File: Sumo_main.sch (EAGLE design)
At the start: 25 parts, among them U1 ATMEGA8U2AU, X1 MINI-USB-SCHIELD-32005-201, X2 ESC1, X3 ESC2, X4 IR Sensor 1, X5 IR Sensor 2, X6 IR Sensor 3, Y1 4MHz

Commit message: Added RS-485
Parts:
- removed X3: ESC2, con-amp-micromatch:MICROMATCH-4
- added C5: 10uF, SparkFun-Capacitors:CAP0603-CAP
- added IC1: MAX3469ESA, maxim:MAX3469ESA
- added R8: 22R, resistor:R-EU_R0603
- X2: value ESC1 -> RS485
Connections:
- new net DE: IC1.DE, IC1.RE/, U1.PD4
- new net N$11: IC1.B, R8.2, X2-4.S
- new net N$12: IC1.A, R8.1, X2-3.S
- new net N$15: C5.1, X2-2.S
- new net RX: IC1.RO, U1.PD2(RX)
- new net TX: IC1.DI, U1.PD3(TX)
- new net V01: U1.PD0, X4-1.S
- new net V02: U1.PD1, X5-1.S
- new net V03: U1.PD5, X6-1.S
- net GND: now also IC1.GND, X2-1.S, X4-2.S, X5-2.S, X6-2.S
- net VCC: now also C5.2, IC1.VCC, X4-3.S, X5-3.S, X6-3.S
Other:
- moved on the sheet: C1, D1, D2, D3, F1, R1, R2, R4, R5, R7, X1G$1, X1S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

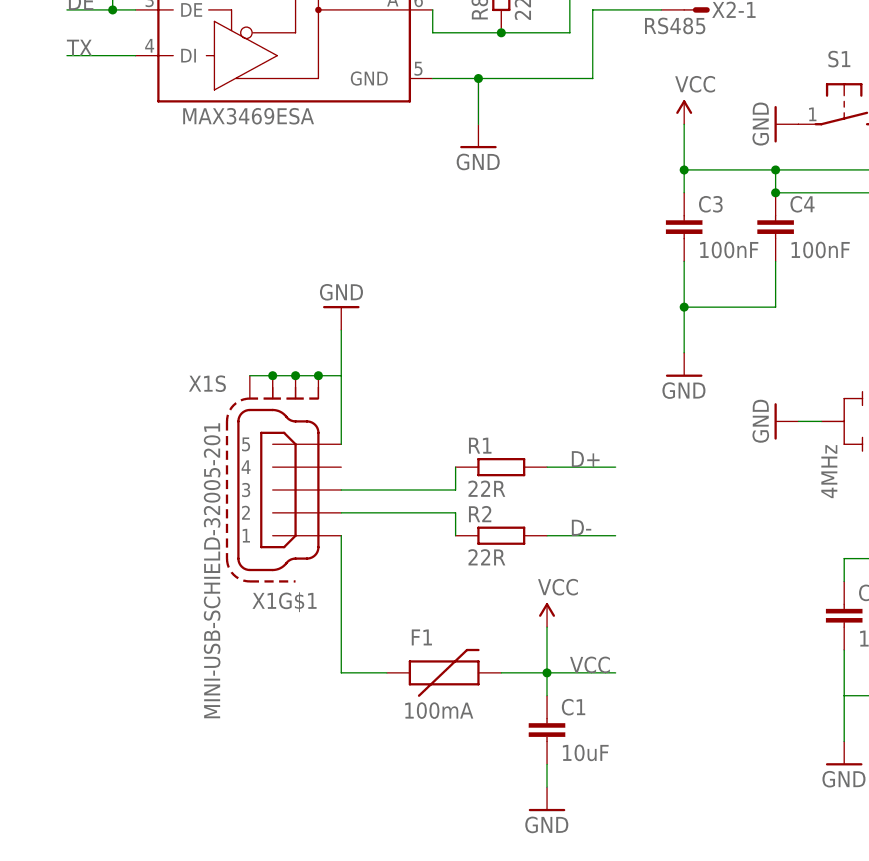
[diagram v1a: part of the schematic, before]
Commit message: Added Non-USB voltage supply.
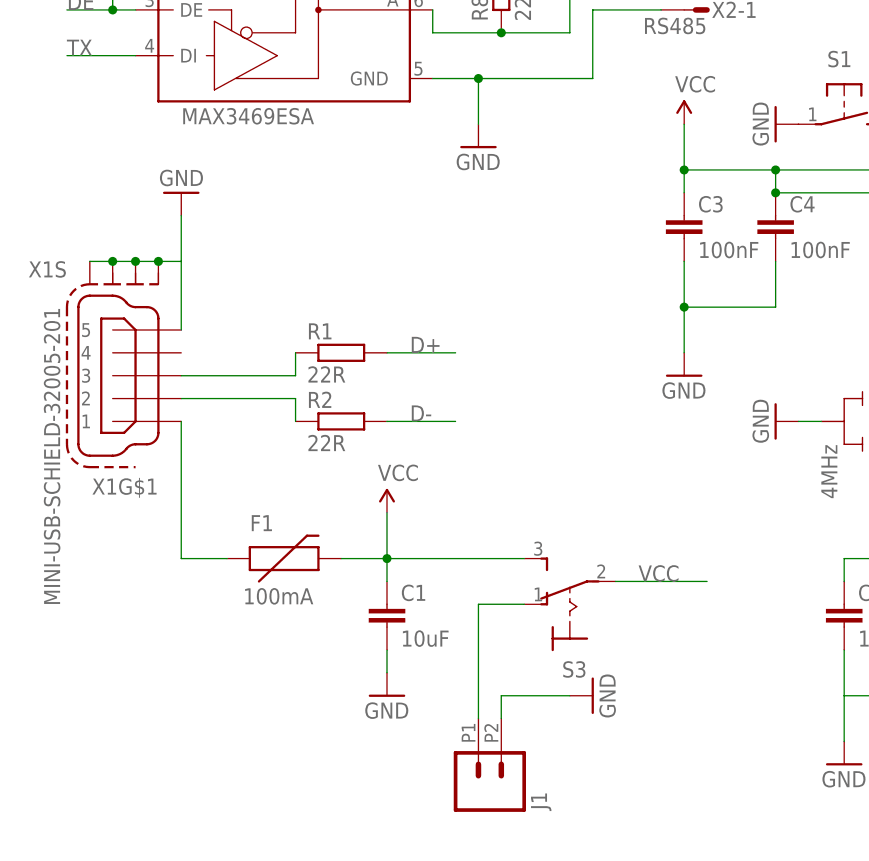
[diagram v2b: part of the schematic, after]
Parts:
- added J1: (no value), SparkFun-Connectors:M022.54MM_SCREWTERM
- added S3: (no value), switch:M9040P
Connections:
- new net N$14: J1.1, S3.O
- net GND: now also J1.2
- net VCC: now also S3.P, S3.S
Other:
- moved on the sheet: C1, F1, R1, R2, X1G$1, X1S
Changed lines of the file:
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@@
 <?xml version="1.0" encoding="utf-8"?>
 <!DOCTYPE eagle SYSTEM "eagle.dtd">
-<eagle version="7.1.0">
+<eagle version="6.5.0">
 <drawing>
 <settings>
@@
 <part name="C5" library="SparkFun-Capacitors" deviceset="CAP" device="0603-CAP" value="10uF"/>
 <part name="SUPPLY6" library="SparkFun-Aesthetics" deviceset="VCC" device=""/>
+<part name="J1" library="SparkFun-Connectors" deviceset="M02" device="2.54MM_SCREWTERM"/>
+<part name="GND10" library="SparkFun-Aesthetics" deviceset="GND" device=""/>
+<part name="S3" library="switch" deviceset="M9040P" device=""/>
 </parts>
 <sheets>
@@
 <instances>
 <instance part="U1" gate="G$1" x="73.66" y="58.42"/>
-<instance part="F1" gate="G$1" x="-5.08" y="25.4"/>
-<instance part="R1" gate="G$1" x="2.54" y="48.26"/>
-<instance part="R2" gate="G$1" x="2.54" y="40.64"/>
-<instance part="C1" gate="G$1" x="7.62" y="17.78"/>
+<instance part="F1" gate="G$1" x="-22.86" y="38.1"/>
+<instance part="R1" gate="G$1" x="-15.24" y="60.96"/>
+<instance part="R2" gate="G$1" x="-15.24" y="53.34"/>
+<instance part="C1" gate="G$1" x="-10.16" y="30.48"/>
 <instance part="C2" gate="G$1" x="40.64" y="30.48"/>
 <instance part="C3" gate="G$1" x="22.86" y="73.66"/>
 <instance part="C4" gate="G$1" x="33.02" y="73.66"/>
-<instance part="SUPPLY1" gate="G$1" x="7.62" y="30.48"/>
-<instance part="GND1" gate="1" x="7.62" y="10.16"/>
+<instance part="SUPPLY1" gate="G$1" x="-10.16" y="43.18"/>
+<instance part="GND1" gate="1" x="-10.16" y="22.86"/>
 <instance part="GND2" gate="1" x="40.64" y="15.24"/>
 <instance part="GND3" gate="1" x="33.02" y="53.34" rot="R270"/>
-<instance part="GND4" gate="1" x="-15.24" y="66.04" rot="R180"/>
-<instance part="X1" gate="G$1" x="-20.32" y="45.72" rot="R180"/>
-<instance part="X1" gate="S" x="-20.32" y="55.88" rot="R180"/>
+<instance part="GND4" gate="1" x="-33.02" y="78.74" rot="R180"/>
+<instance part="X1" gate="G$1" x="-38.1" y="58.42" rot="R180"/>
+<instance part="X1" gate="S" x="-38.1" y="68.58" rot="R180"/>
 <instance part="Y1" gate="G$1" x="45.72" y="53.34" rot="R270"/>
 <instance part="SUPPLY2" gate="G$1" x="22.86" y="86.36"/>
@@
 <instance part="C5" gate="G$1" x="20.32" y="114.3" rot="R90"/>
 <instance part="SUPPLY6" gate="G$1" x="25.4" y="114.3" rot="R270"/>
+<instance part="J1" gate="G$1" x="0" y="12.7" rot="MR90"/>
+<instance part="GND10" gate="1" x="12.7" y="22.86" rot="R90"/>
+<instance part="S3" gate="1" x="10.16" y="33.02" rot="R90"/>
 </instances>
 <busses>
@@
 <segment>
 <pinref part="R1" gate="G$1" pin="1"/>
-<wire x1="-2.54" y1="45.72" x2="-2.54" y2="48.26" width="0.1524" layer="91"/>
+<wire x1="-20.32" y1="58.42" x2="-20.32" y2="60.96" width="0.1524" layer="91"/>
 <pinref part="X1" gate="G$1" pin="3"/>
-<wire x1="-15.24" y1="45.72" x2="-2.54" y2="45.72" width="0.1524" layer="91"/>
+<wire x1="-33.02" y1="58.42" x2="-20.32" y2="58.42" width="0.1524" layer="91"/>
 </segment>
 </net>
@@
 <segment>
 <pinref part="R2" gate="G$1" pin="1"/>
-<wire x1="-15.24" y1="43.18" x2="-2.54" y2="43.18" width="0.1524" layer="91"/>
-<wire x1="-2.54" y1="43.18" x2="-2.54" y2="40.64" width="0.1524" layer="91"/>
+<wire x1="-33.02" y1="55.88" x2="-20.32" y2="55.88" width="0.1524" layer="91"/>
+<wire x1="-20.32" y1="55.88" x2="-20.32" y2="53.34" width="0.1524" layer="91"/>
 <pinref part="X1" gate="G$1" pin="2"/>
 </segment>
@@
 <segment>
 <pinref part="R1" gate="G$1" pin="2"/>
-<wire x1="7.62" y1="48.26" x2="15.24" y2="48.26" width="0.1524" layer="91"/>
-<label x="10.16" y="48.26" size="1.778" layer="95"/>
+<wire x1="-10.16" y1="60.96" x2="-2.54" y2="60.96" width="0.1524" layer="91"/>
+<label x="-7.62" y="60.96" size="1.778" layer="95"/>
 </segment>
 <segment>
@@
 <segment>
 <pinref part="R2" gate="G$1" pin="2"/>
-<wire x1="7.62" y1="40.64" x2="15.24" y2="40.64" width="0.1524" layer="91"/>
-<label x="10.16" y="40.64" size="1.778" layer="95"/>
+<wire x1="-10.16" y1="53.34" x2="-2.54" y2="53.34" width="0.1524" layer="91"/>
+<label x="-7.62" y="53.34" size="1.778" layer="95"/>
 </segment>
 <segment>
@@
 <net name="N$3" class="0">
 <segment>
-<wire x1="-15.24" y1="40.64" x2="-15.24" y2="25.4" width="0.1524" layer="91"/>
+<wire x1="-33.02" y1="53.34" x2="-33.02" y2="38.1" width="0.1524" layer="91"/>
 <pinref part="F1" gate="G$1" pin="1"/>
-<wire x1="-15.24" y1="25.4" x2="-10.16" y2="25.4" width="0.1524" layer="91"/>
+<wire x1="-33.02" y1="38.1" x2="-27.94" y2="38.1" width="0.1524" layer="91"/>
 <pinref part="X1" gate="G$1" pin="1"/>
 </segment>
@@
 <pinref part="F1" gate="G$1" pin="2"/>
 <pinref part="SUPPLY1" gate="G$1" pin="VCC"/>
-<wire x1="2.54" y1="25.4" x2="7.62" y2="25.4" width="0.1524" layer="91"/>
-<wire x1="7.62" y1="25.4" x2="7.62" y2="30.48" width="0.1524" layer="91"/>
+<wire x1="-15.24" y1="38.1" x2="-10.16" y2="38.1" width="0.1524" layer="91"/>
+<wire x1="-10.16" y1="38.1" x2="-10.16" y2="43.18" width="0.1524" layer="91"/>
 <pinref part="C1" gate="G$1" pin="1"/>
-<wire x1="7.62" y1="22.86" x2="7.62" y2="25.4" width="0.1524" layer="91"/>
-<wire x1="7.62" y1="25.4" x2="15.24" y2="25.4" width="0.1524" layer="91"/>
-<label x="10.16" y="25.4" size="1.778" layer="95"/>
-<junction x="7.62" y="25.4"/>
+<wire x1="-10.16" y1="35.56" x2="-10.16" y2="38.1" width="0.1524" layer="91"/>
+<junction x="-10.16" y="38.1"/>
+<pinref part="S3" gate="1" pin="S"/>
+<wire x1="-10.16" y1="38.1" x2="5.08" y2="38.1" width="0.1524" layer="91"/>
 </segment>
 <segment>
@@
 <junction x="25.4" y="114.3"/>
 </segment>
+<segment>
+<pinref part="S3" gate="1" pin="P"/>
+<wire x1="15.24" y1="35.56" x2="25.4" y2="35.56" width="0.1524" layer="91"/>
+<label x="17.78" y="35.56" size="1.778" layer="95"/>
+</segment>
 </net>
 <net name="GND" class="0">
@@
 <pinref part="C1" gate="G$1" pin="2"/>
 <pinref part="GND1" gate="1" pin="GND"/>
-<wire x1="7.62" y1="15.24" x2="7.62" y2="12.7" width="0.1524" layer="91"/>
+<wire x1="-10.16" y1="27.94" x2="-10.16" y2="25.4" width="0.1524" layer="91"/>
 </segment>
 <segment>
 <pinref part="X1" gate="G$1" pin="5"/>
-<wire x1="-15.24" y1="50.8" x2="-15.24" y2="58.42" width="0.1524" layer="91"/>
+<wire x1="-33.02" y1="63.5" x2="-33.02" y2="71.12" width="0.1524" layer="91"/>
 <pinref part="X1" gate="S" pin="S1"/>
-<wire x1="-15.24" y1="58.42" x2="-17.78" y2="58.42" width="0.1524" layer="91"/>
+<wire x1="-33.02" y1="71.12" x2="-35.56" y2="71.12" width="0.1524" layer="91"/>
 <pinref part="X1" gate="S" pin="S2"/>
 <pinref part="X1" gate="S" pin="S3"/>
 <pinref part="X1" gate="S" pin="S4"/>
-<wire x1="-25.4" y1="58.42" x2="-22.86" y2="58.42" width="0.1524" layer="91"/>
-<wire x1="-22.86" y1="58.42" x2="-20.32" y2="58.42" width="0.1524" layer="91"/>
-<wire x1="-20.32" y1="58.42" x2="-17.78" y2="58.42" width="0.1524" layer="91"/>
-<wire x1="-15.24" y1="58.42" x2="-15.24" y2="63.5" width="0.1524" layer="91"/>
-<junction x="-22.86" y="58.42"/>
-<junction x="-20.32" y="58.42"/>
-<junction x="-17.78" y="58.42"/>
+<wire x1="-43.18" y1="71.12" x2="-40.64" y2="71.12" width="0.1524" layer="91"/>
+<wire x1="-40.64" y1="71.12" x2="-38.1" y2="71.12" width="0.1524" layer="91"/>
+<wire x1="-38.1" y1="71.12" x2="-35.56" y2="71.12" width="0.1524" layer="91"/>
+<wire x1="-33.02" y1="71.12" x2="-33.02" y2="76.2" width="0.1524" layer="91"/>
+<junction x="-40.64" y="71.12"/>
+<junction x="-38.1" y="71.12"/>
+<junction x="-35.56" y="71.12"/>
 <pinref part="GND4" gate="1" pin="GND"/>
 </segment>
@@
 <wire x1="12.7" y1="99.06" x2="12.7" y2="91.44" width="0.1524" layer="91"/>
 </segment>
+<segment>
+<pinref part="J1" gate="G$1" pin="2"/>
+<pinref part="GND10" gate="1" pin="GND"/>
+<wire x1="2.54" y1="20.32" x2="2.54" y2="22.86" width="0.1524" layer="91"/>
+<wire x1="2.54" y1="22.86" x2="10.16" y2="22.86" width="0.1524" layer="91"/>
+</segment>
 </net>
 <net name="N$5" class="0">
@@
 </segment>
 </net>
+<net name="N$14" class="0">
+<segment>
+<pinref part="J1" gate="G$1" pin="1"/>
+<wire x1="0" y1="20.32" x2="0" y2="33.02" width="0.1524" layer="91"/>
+<pinref part="S3" gate="1" pin="O"/>
+<wire x1="0" y1="33.02" x2="5.08" y2="33.02" width="0.1524" layer="91"/>
+</segment>
+</net>

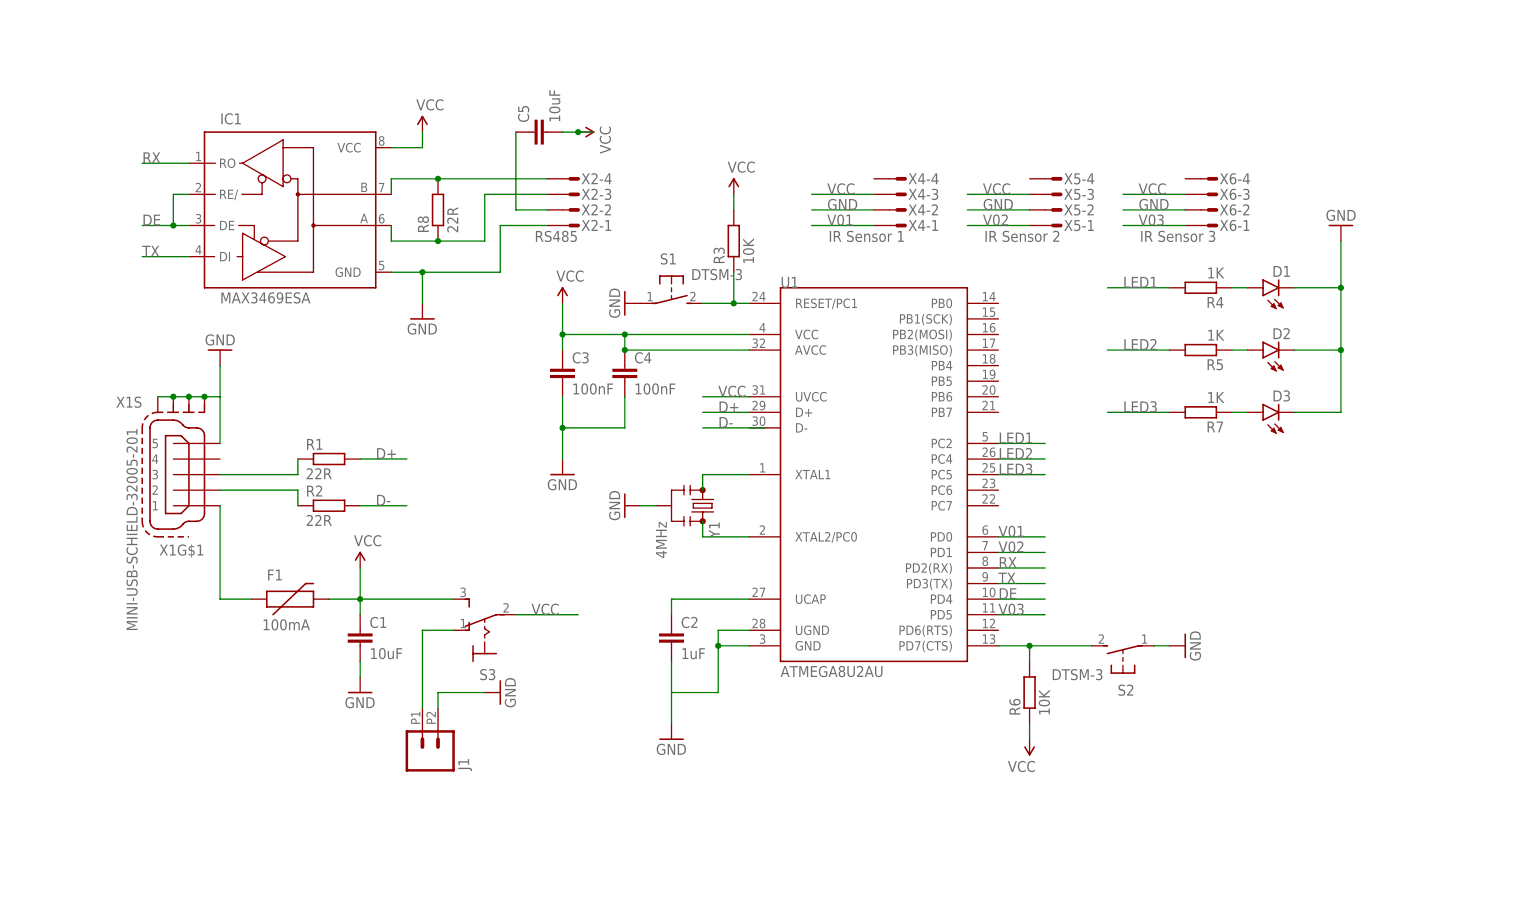
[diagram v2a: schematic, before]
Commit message: Changed RS485 module, added start module and power voltage regulator.
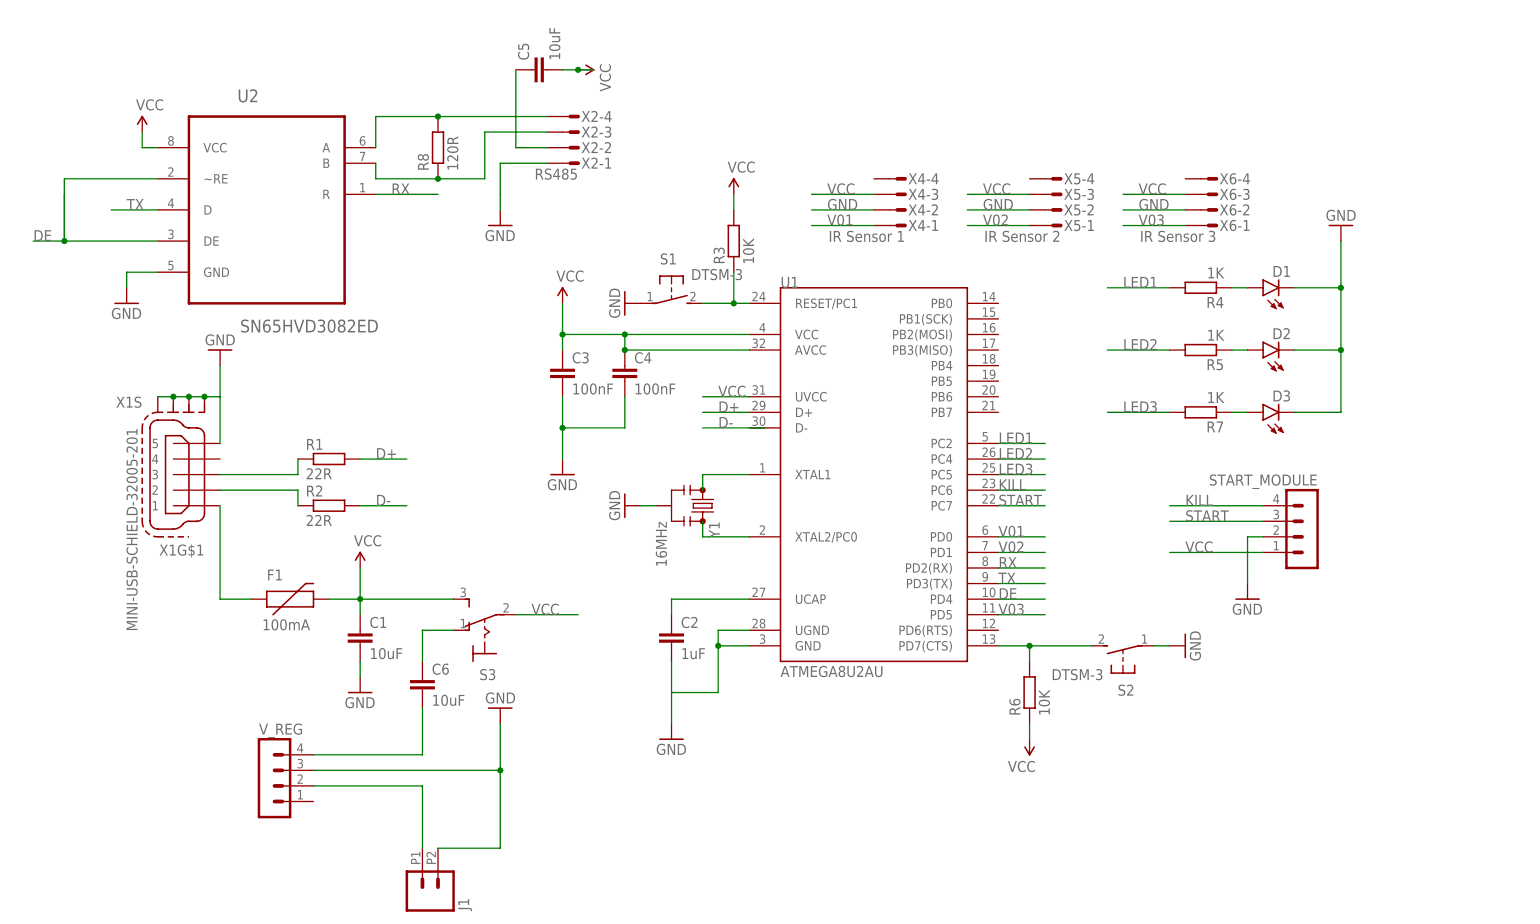
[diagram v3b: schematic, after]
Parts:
- removed IC1: MAX3469ESA, maxim:MAX3469ESA
- added C6: 10uF, SparkFun-Capacitors:CAP0603-CAP
- added START_MODULE, V_REG: (no value), con-lstb:MA04-1
- added U2: SN65HVD3082ED, SN65HVD3082ED:SN65HVD3082ED
- R8: value 22R -> 120R
- Y1: value 4MHz -> 16MHz
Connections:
- new net KILL: START_MODULE.4, U1.PC6
- new net N$21: C6.2, V_REG.4
- new net N$23: J1.1, V_REG.2
- new net START: START_MODULE.3, U1.PC7
- net DE: now also U2.DE, U2.~RE; no longer IC1.DE, IC1.RE/
- net GND: now also START_MODULE.2, U2.GND, V_REG.3; no longer IC1.GND
- net N$11: no longer IC1.B
- net N$12: no longer IC1.A
- net N$14: now also C6.1; no longer J1.1
- net RX: now also U2.R; no longer IC1.RO
- net TX: now also U2.D; no longer IC1.DI
- net VCC: now also START_MODULE.1, U2.VCC; no longer IC1.VCC
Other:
- moved on the sheet: C5, J1, R8, X2-1, X2-2, X2-3, X2-4
